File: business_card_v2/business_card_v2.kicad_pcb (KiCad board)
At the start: 2 copper layers, 85.6 x 54 mm, 181 parts, among them M1 CH32X035F7P6, P1 AMS1117-3.3, SW3 SW_Push, U1 CH32V006F8P6, U2 CH32V006F8P6, U3 CH32V006F8P6, U4 CH32V006F8P6, U5 CH32V006F8P6, U6 CH32V006F8P6, U7 CH32V006F8P6, U8 CH32V006F8P6

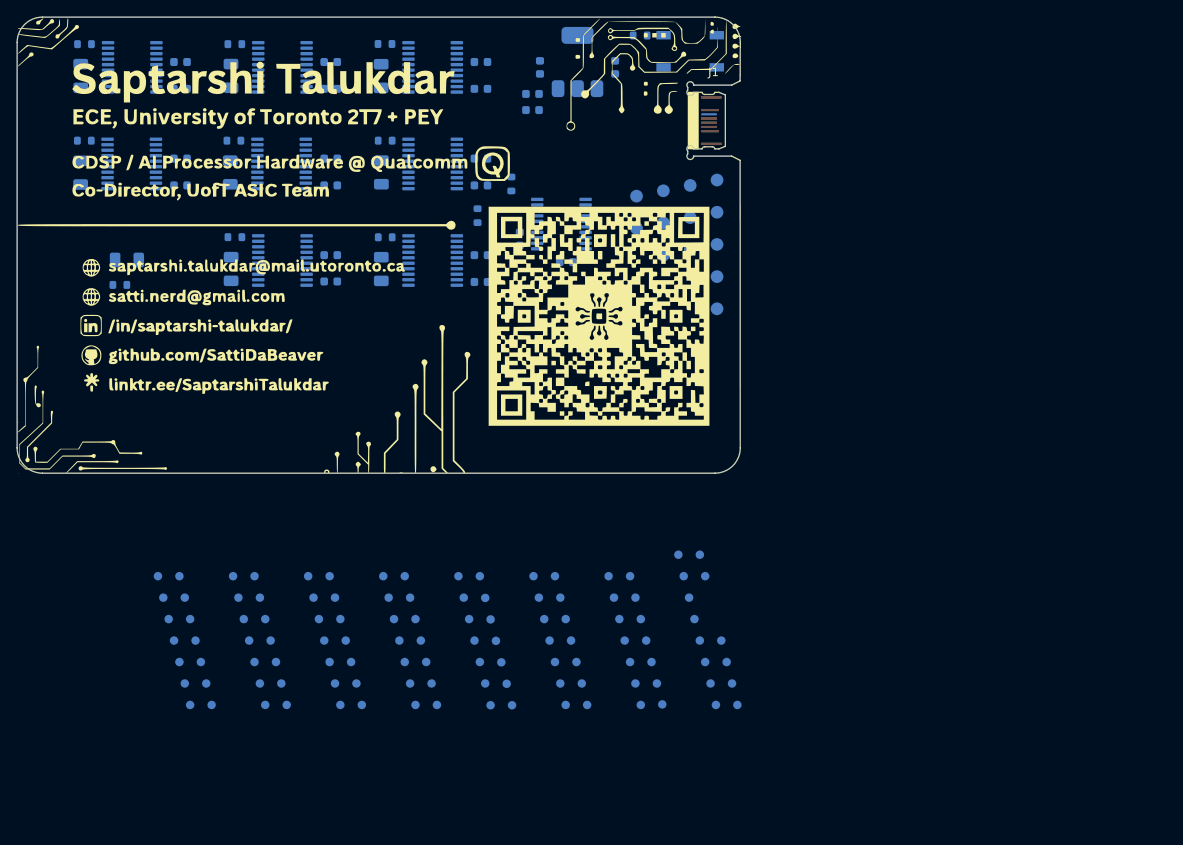
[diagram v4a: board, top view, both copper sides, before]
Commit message: wired all GPIO
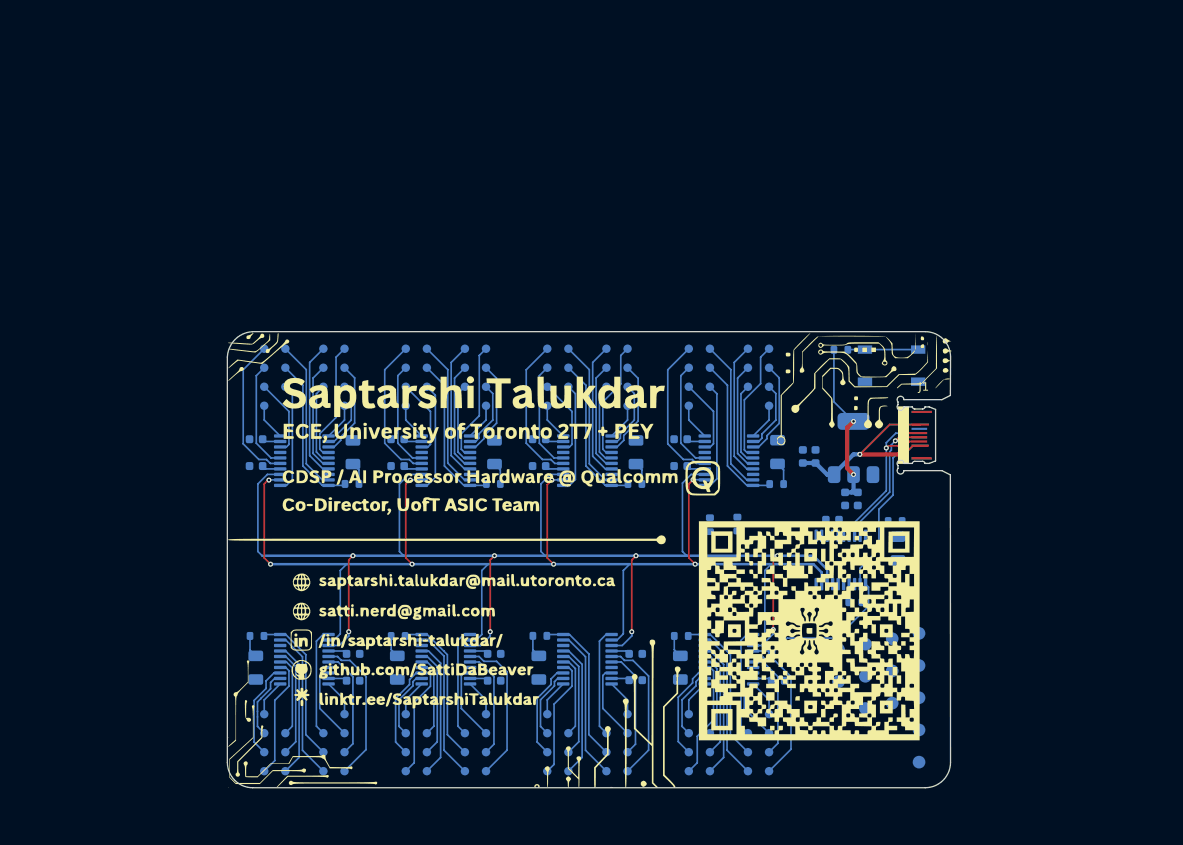
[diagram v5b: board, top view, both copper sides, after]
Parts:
- moved D9 97.4 mm to (138.2, 101.4), turned to 90 degrees
- moved R11 95.9 mm to (137.9, 98.2), turned to 0 degrees
- moved D7 79.4 mm to (79.0, 115.5)
- moved C19 79.3 mm to (90.5, 117.0)
- moved C18 79.3 mm to (90.5, 113.9)
- moved R9 79.3 mm to (79.1, 111.8)
- moved U7 79.3 mm to (84.8, 114.5)
- moved D5 79.2 mm to (112.5, 115.5)
- moved C13 79.0 mm to (124.1, 113.9)
- moved C14 79.0 mm to (124.1, 117.0)
- moved R7 79.0 mm to (112.6, 111.7)
- moved U5 79.0 mm to (118.2, 114.5)
- moved R3 69.7 mm to (123.9, 93.8), turned to 0 degrees
- moved D1 64.7 mm to (124.0, 90.0), turned to -90 degrees
- moved C10 62.6 mm to (132.0, 95.5)
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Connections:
- M1 pad 1: /NRST_S1 -> /NRST_S5
- M1 pad 10: /NRST_S5 -> /NRST_S4
- M1 pad 12: /NRST_S6 -> /NRST_S3
- M1 pad 13: /NRST_S7 -> /NRST_S2
- M1 pad 14: /NRST_S8 -> /NRST_S1
- M1 pad 5: /NRST_S2 -> /NRST_S6
- M1 pad 6: /NRST_S3 -> /NRST_S7
- M1 pad 7: /NRST_S4 -> /NRST_S8
- S1_GP0 pad 1: Net-(U1-PD4) -> Net-(U1-PC0)
- S1_GP1 pad 1: Net-(U1-PA1) -> Net-(U1-PD0)
- S1_GP10 pad 1: Net-(U1-PC6) -> Net-(U1-PC4)
- S1_GP11 pad 1: Net-(U1-PC7) -> Net-(U1-PC3)
- S1_GP12 pad 1: Net-(U1-PD2) -> Net-(U1-PC2)
- S1_GP13 pad 1: Net-(U1-PD3) -> Net-(U1-PC1)
- S1_GP3 pad 1: Net-(U1-PD0) -> Net-(U1-PA1)
- S1_GP4 pad 1: Net-(U1-PC0) -> Net-(U1-PD2)
- S1_GP5 pad 1: Net-(U1-PC1) -> Net-(U1-PD3)
- S1_GP6 pad 1: Net-(U1-PC2) -> Net-(U1-PD4)
- S1_GP7 pad 1: Net-(U1-PC3) -> Net-(U1-PC5)
- S1_GP8 pad 1: Net-(U1-PC4) -> Net-(U1-PC6)
- S1_GP9 pad 1: Net-(U1-PC5) -> Net-(U1-PC7)
- S2_GP0 pad 1: Net-(U2-PD4) -> Net-(U2-PC0)
- S2_GP1 pad 1: Net-(U2-PA1) -> Net-(U2-PD0)
- S2_GP10 pad 1: Net-(U2-PC6) -> Net-(U2-PC4)
- S2_GP11 pad 1: Net-(U2-PC7) -> Net-(U2-PC3)
- S2_GP12 pad 1: Net-(U2-PD2) -> Net-(U2-PC2)
- S2_GP13 pad 1: Net-(U2-PD3) -> Net-(U2-PC1)
- S2_GP3 pad 1: Net-(U2-PD0) -> Net-(U2-PA1)
- S2_GP4 pad 1: Net-(U2-PC0) -> Net-(U2-PD2)
- S2_GP5 pad 1: Net-(U2-PC1) -> Net-(U2-PD3)
- S2_GP6 pad 1: Net-(U2-PC2) -> Net-(U2-PD4)
- S2_GP7 pad 1: Net-(U2-PC3) -> Net-(U2-PC5)
- S2_GP8 pad 1: Net-(U2-PC4) -> Net-(U2-PC6)
- S2_GP9 pad 1: Net-(U2-PC5) -> Net-(U2-PC7)
- S3_GP0 pad 1: Net-(U3-PD4) -> Net-(U3-PC0)
- S3_GP1 pad 1: Net-(U3-PA1) -> Net-(U3-PD0)
- S3_GP10 pad 1: Net-(U3-PC6) -> Net-(U3-PC4)
- S3_GP11 pad 1: Net-(U3-PC7) -> Net-(U3-PC3)
- S3_GP12 pad 1: Net-(U3-PD2) -> Net-(U3-PC2)
- S3_GP13 pad 1: Net-(U3-PD3) -> Net-(U3-PC1)
- S3_GP3 pad 1: Net-(U3-PD0) -> Net-(U3-PA1)
- S3_GP4 pad 1: Net-(U3-PC0) -> Net-(U3-PD2)
- S3_GP5 pad 1: Net-(U3-PC1) -> Net-(U3-PD3)
- S3_GP6 pad 1: Net-(U3-PC2) -> Net-(U3-PD4)
- S3_GP7 pad 1: Net-(U3-PC3) -> Net-(U3-PC5)
- S3_GP8 pad 1: Net-(U3-PC4) -> Net-(U3-PC6)
- S3_GP9 pad 1: Net-(U3-PC5) -> Net-(U3-PC7)
- S4_GP0 pad 1: Net-(U4-PD4) -> Net-(U4-PC0)
- S4_GP1 pad 1: Net-(U4-PA1) -> Net-(U4-PD0)
- S4_GP10 pad 1: Net-(U4-PC6) -> Net-(U4-PC4)
- S4_GP11 pad 1: Net-(U4-PC7) -> Net-(U4-PC3)
- S4_GP12 pad 1: Net-(U4-PD2) -> Net-(U4-PC2)
- S4_GP13 pad 1: Net-(U4-PD3) -> Net-(U4-PC1)
- S4_GP3 pad 1: Net-(U4-PD0) -> Net-(U4-PA1)
- S4_GP4 pad 1: Net-(U4-PC0) -> Net-(U4-PD2)
- S4_GP5 pad 1: Net-(U4-PC1) -> Net-(U4-PD3)
- S4_GP6 pad 1: Net-(U4-PC2) -> Net-(U4-PD4)
- S4_GP7 pad 1: Net-(U4-PC3) -> Net-(U4-PC5)
- S4_GP8 pad 1: Net-(U4-PC4) -> Net-(U4-PC6)
- S4_GP9 pad 1: Net-(U4-PC5) -> Net-(U4-PC7)
- S5_GP0 pad 1: Net-(U5-PD4) -> Net-(U5-PC0)
- S5_GP1 pad 1: Net-(U5-PA1) -> Net-(U5-PD0)
- S5_GP10 pad 1: Net-(U5-PC6) -> Net-(U5-PC4)
- S5_GP11 pad 1: Net-(U5-PC7) -> Net-(U5-PC3)
- S5_GP12 pad 1: Net-(U5-PD2) -> Net-(U5-PC2)
- S5_GP13 pad 1: Net-(U5-PD3) -> Net-(U5-PC1)
- S5_GP3 pad 1: Net-(U5-PD0) -> Net-(U5-PA1)
- S5_GP4 pad 1: Net-(U5-PC0) -> Net-(U5-PD2)
- S5_GP5 pad 1: Net-(U5-PC1) -> Net-(U5-PD3)
- S5_GP6 pad 1: Net-(U5-PC2) -> Net-(U5-PD4)
- S5_GP7 pad 1: Net-(U5-PC3) -> Net-(U5-PC5)
- S5_GP8 pad 1: Net-(U5-PC4) -> Net-(U5-PC6)
- S5_GP9 pad 1: Net-(U5-PC5) -> Net-(U5-PC7)
- S6_GP0 pad 1: Net-(U6-PD4) -> Net-(U6-PC0)
- S6_GP1 pad 1: Net-(U6-PA1) -> Net-(U6-PD0)
- S6_GP10 pad 1: Net-(U6-PC6) -> Net-(U6-PC4)
- S6_GP11 pad 1: Net-(U6-PC7) -> Net-(U6-PC3)
- S6_GP12 pad 1: Net-(U6-PD2) -> Net-(U6-PC2)
- S6_GP13 pad 1: Net-(U6-PD3) -> Net-(U6-PC1)
- S6_GP3 pad 1: Net-(U6-PD0) -> Net-(U6-PA1)
- S6_GP4 pad 1: Net-(U6-PC0) -> Net-(U6-PD2)
- S6_GP5 pad 1: Net-(U6-PC1) -> Net-(U6-PD3)
- S6_GP6 pad 1: Net-(U6-PC2) -> Net-(U6-PD4)
- S6_GP7 pad 1: Net-(U6-PC3) -> Net-(U6-PC5)
- S6_GP8 pad 1: Net-(U6-PC4) -> Net-(U6-PC6)
- S6_GP9 pad 1: Net-(U6-PC5) -> Net-(U6-PC7)
- S7_GP0 pad 1: Net-(U7-PD4) -> Net-(U7-PC0)
- S7_GP1 pad 1: Net-(U7-PA1) -> Net-(U7-PD0)
- S7_GP10 pad 1: Net-(U7-PC6) -> Net-(U7-PC4)
- S7_GP11 pad 1: Net-(U7-PC7) -> Net-(U7-PC3)
- S7_GP12 pad 1: Net-(U7-PD2) -> Net-(U7-PC2)
- S7_GP13 pad 1: Net-(U7-PD3) -> Net-(U7-PC1)
- S7_GP3 pad 1: Net-(U7-PD0) -> Net-(U7-PA1)
- S7_GP4 pad 1: Net-(U7-PC0) -> Net-(U7-PD2)
- S7_GP5 pad 1: Net-(U7-PC1) -> Net-(U7-PD3)
- S7_GP6 pad 1: Net-(U7-PC2) -> Net-(U7-PD4)
- S7_GP7 pad 1: Net-(U7-PC3) -> Net-(U7-PC5)
- S7_GP8 pad 1: Net-(U7-PC4) -> Net-(U7-PC6)
- S7_GP9 pad 1: Net-(U7-PC5) -> Net-(U7-PC7)
- S8_GP0 pad 1: Net-(U8-PD4) -> Net-(U8-PC0)
- S8_GP1 pad 1: Net-(U8-PA1) -> Net-(U8-PD0)
- S8_GP10 pad 1: Net-(U8-PC6) -> Net-(U8-PC4)
- S8_GP11 pad 1: Net-(U8-PC7) -> Net-(U8-PC3)
- S8_GP12 pad 1: Net-(U8-PD2) -> Net-(U8-PC2)
- S8_GP13 pad 1: Net-(U8-PD3) -> Net-(U8-PC1)
- S8_GP3 pad 1: Net-(U8-PD0) -> Net-(U8-PA1)
- S8_GP4 pad 1: Net-(U8-PC0) -> Net-(U8-PD2)
- S8_GP5 pad 1: Net-(U8-PC1) -> Net-(U8-PD3)
- S8_GP6 pad 1: Net-(U8-PC2) -> Net-(U8-PD4)
- S8_GP7 pad 1: Net-(U8-PC3) -> Net-(U8-PC5)
- S8_GP8 pad 1: Net-(U8-PC4) -> Net-(U8-PC6)
- S8_GP9 pad 1: Net-(U8-PC5) -> Net-(U8-PC7)
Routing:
- net /BUS_MOSI: track 0.00 -> 167.2 mm, vias 0 -> 8
- net /BUS_MISO: track 0.00 -> 156.5 mm, vias 0 -> 8
- net +3.3V: track 0.00 -> 38.3 mm, vias 0 -> 2
- net +5V: track 0.00 -> 35.4 mm, vias 0 -> 2
- net /D+: track 0.00 -> 21.7 mm, vias 0 -> 1
- net /CC1: track 0.00 -> 20.5 mm, vias 0 -> 1
- net /D-: track 0.00 -> 19.6 mm, vias 0 -> 1
- net /NRST_S5: track 0.00 -> 18.9 mm
- net Net-(U1-PD3): track 0.00 -> 18.5 mm
- net Net-(U4-PD3): track 0.00 -> 18.5 mm
- net Net-(U6-PD3): track 0.00 -> 18.5 mm
- net Net-(U2-PD3): track 0.00 -> 18.5 mm
- net Net-(U3-PD3): track 0.00 -> 18.5 mm
- net Net-(U7-PD3): track 0.00 -> 18.5 mm
- net Net-(U5-PD3): track 0.00 -> 18.5 mm
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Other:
- outline, holes or cut-outs redrawn

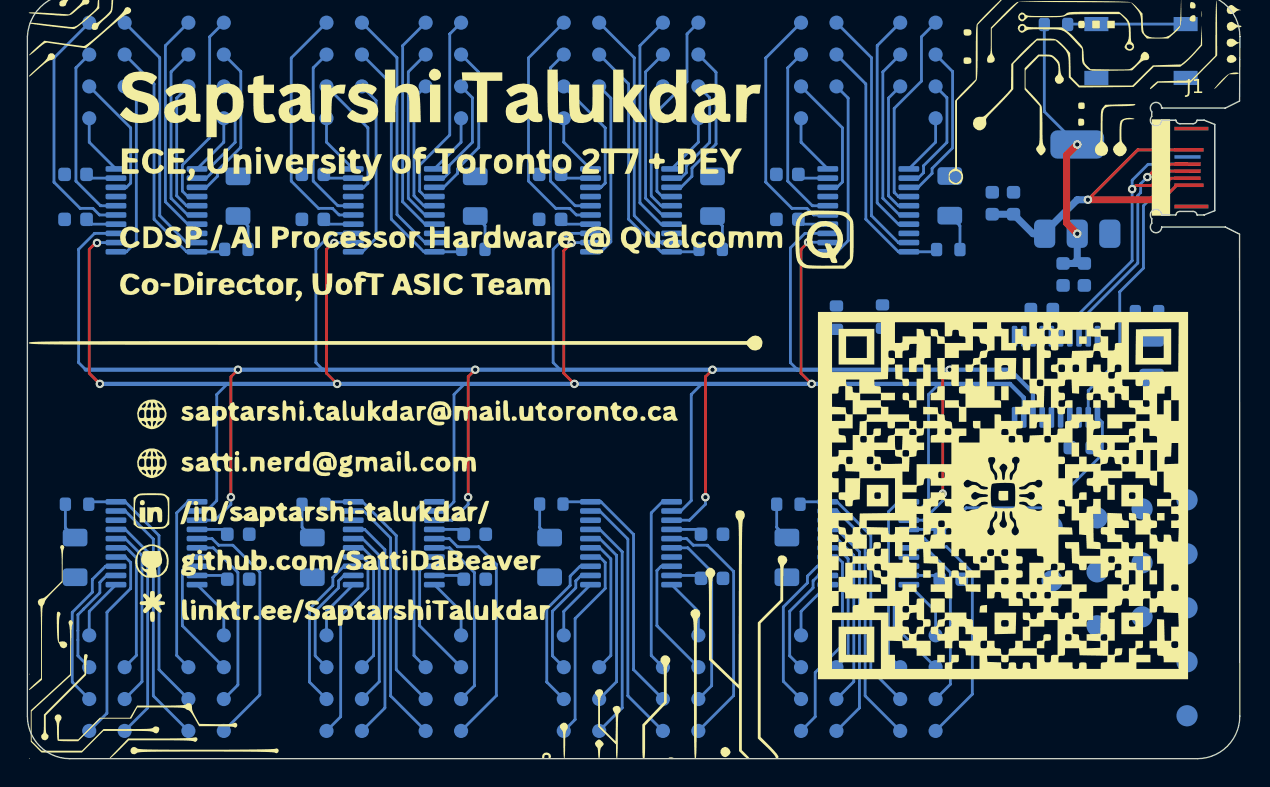
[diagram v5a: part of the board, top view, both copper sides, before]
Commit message: added reset wires and bus
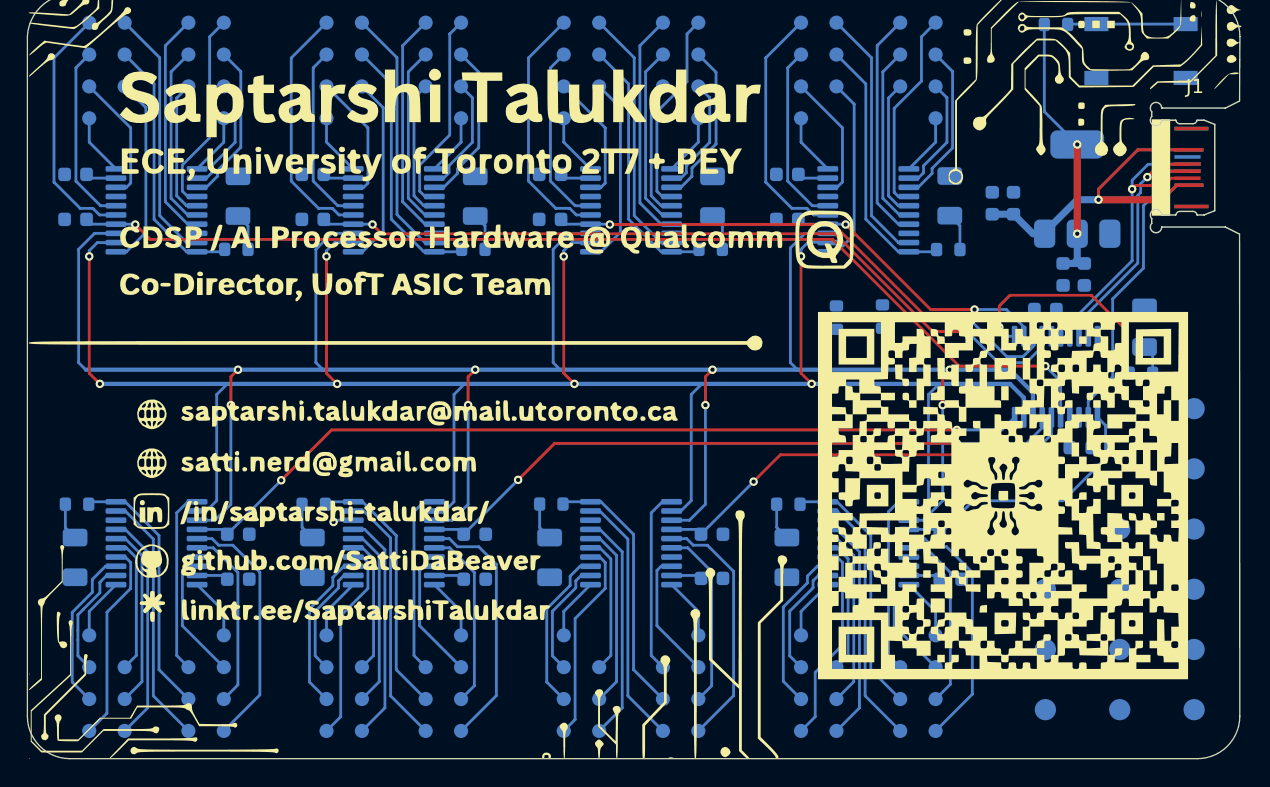
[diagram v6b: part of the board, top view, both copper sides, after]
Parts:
- moved P7 10.8 mm to (141.2, 109.2)
- moved P8 10.3 mm to (136.0, 126.2)
- moved P4 9.43 mm to (136.0, 122.0)
- moved P3 7.10 mm to (130.8, 117.8)
- moved P6 6.95 mm to (130.8, 126.2)
- moved P5 6.58 mm to (130.8, 122.0)
- moved GND 6.46 mm to (141.2, 105.0)
- moved MCLK 5.58 mm to (141.2, 113.5)
- moved R11 4.37 mm to (137.5, 102.5)
- moved MDIO 2.55 mm to (141.2, 117.8)
- moved P2 2.44 mm to (136.0, 117.8)
- moved D9 2.21 mm to (137.8, 99.2), turned to -90 degrees
- moved P1 2.12 mm to (136.0, 113.5)
- moved BMOSI 1.00 mm to (141.2, 122.0)
- moved BMISO 0.66 mm to (141.2, 126.2)
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- renumbered TP15 to BMISO, TP14 to BMOSI, TP13 to GND, TP12 to MCLK, TP11 to MDIO, TP1 to P1, TP2 to P2, TP3 to P3, TP4 to P4, TP5 to P5, TP6 to P6, TP7 to P7, TP8 to P8
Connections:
- M1 pad 10: /NRST_S4 -> /NRST_S8
- M1 pad 12: /NRST_S3 -> /NRST_S1
- M1 pad 14: /NRST_S1 -> /NRST_S3
- M1 pad 5: /NRST_S6 -> /NRST_S4
- M1 pad 6: /NRST_S7 -> /NRST_S6
- M1 pad 7: /NRST_S8 -> /NRST_S7
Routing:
- net /NRST_S4: track 2.22 -> 76.0 mm, vias 0 -> 2
- net /NRST_S8: track 2.27 -> 61.3 mm, vias 0 -> 2
- net /NRST_S3: track 2.22 -> 56.1 mm, vias 0 -> 2
- net /NRST_S7: track 2.22 -> 46.9 mm, vias 0 -> 2
- net /NRST_S2: track 2.22 -> 38.4 mm, vias 0 -> 2
- net /NRST_S6: track 2.22 -> 31.1 mm, vias 0 -> 2
- net /NRST_S1: track 2.22 -> 19.7 mm, vias 0 -> 2
- net Net-(M1-PA5): track 0.00 -> 16.3 mm, vias 0 -> 2
- net Net-(D9-A): track 0.00 -> 2.09 mm
- net /SWIO_N7: track 0.00 -> 1.44 mm, vias 0 -> 1
- net +3.3V: track 38.3 -> 37.7 mm
- net +5V: track 35.4 -> 34.8 mm
- net Net-(U4-PD4): track 13.0 -> 13.6 mm
- net Net-(U2-PD4): track 13.0 -> 13.6 mm

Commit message: finalized PCB
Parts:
- removed the G*** at (101.8, 102.8)
- added G***: LOGO, LOGO, F.Cu at (102.0, 103.0)
- added G***: LOGO, LOGO, B.Cu at (136.5, 120.5)
- added GND: GND, TestPoint:TestPoint_Pad_D1.5mm, B.Cu at (61.0, 108.0)
- moved BMISO 83.1 mm to (61.0, 104.5)
- moved BMOSI 83.0 mm to (61.0, 101.0)
- moved P8 74.8 mm to (62.4, 113.0)
- moved P4 68.9 mm to (73.7, 92.5)
- moved P7 62.4 mm to (79.0, 113.0)
- moved P3 47.7 mm to (90.3, 92.5)
- moved P2 38.5 mm to (107.0, 92.5)
- moved P6 37.3 mm to (95.9, 113.0)
- moved P1 24.3 mm to (123.8, 92.5)
- moved P5 20.3 mm to (112.5, 113.0)
- moved GND 10.5 mm to (134.5, 113.0)
- moved D1 8.70 mm to (118.2, 96.5), turned to 0 degrees
- moved D6 8.68 mm to (101.5, 109.0), turned to 180 degrees
- moved D8 8.68 mm to (68.0, 109.0), turned to 180 degrees
- moved D2 8.68 mm to (101.5, 96.5), turned to 0 degrees
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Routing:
- net +3.3V: track 37.7 -> 250.7 mm, vias 2 -> 13
- net GND: track 0.00 -> 53.4 mm, vias 0 -> 58
- net /NRST_MASTER: track 10.5 -> 53.9 mm, vias 0 -> 4
- net /SWDIO_M: track 0.00 -> 16.3 mm, vias 0 -> 2
- net /SWCLK_M: track 0.00 -> 13.5 mm, vias 0 -> 2
- net /BUS_MISO: track 156.4 -> 161.5 mm
- net /BUS_MOSI: track 167.2 -> 171.9 mm
- net /SWIO_N5: track 0.00 -> 2.94 mm
- net /SWIO_N4: track 0.00 -> 2.90 mm
- net /SWIO_N6: track 0.00 -> 2.82 mm
- net /SWIO_N8: track 0.00 -> 2.80 mm
- net /SWIO_N3: track 0.00 -> 2.73 mm
- net /SWIO_N1: track 0.00 -> 2.70 mm
- net /SWIO_N2: track 0.00 -> 2.69 mm
- net /SWIO_N7: track 1.44 -> 2.94 mm, vias 1 -> 0
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- added copper zone on B.Cu, net GND
- added copper zone on F.Cu, net GND
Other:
- board text added: "RISC-V Supercluster"
- board text added: "Supercluster v1.0"
- board text removed: "Compute Module"
